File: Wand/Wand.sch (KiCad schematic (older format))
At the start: 27 parts, among them IC1 ATMEGA328-MMH, J1 ACJS-NH35, P1 ISP, P2 BASE, U1 OPA336U, U2 MPU-6050, Y1 16MHz

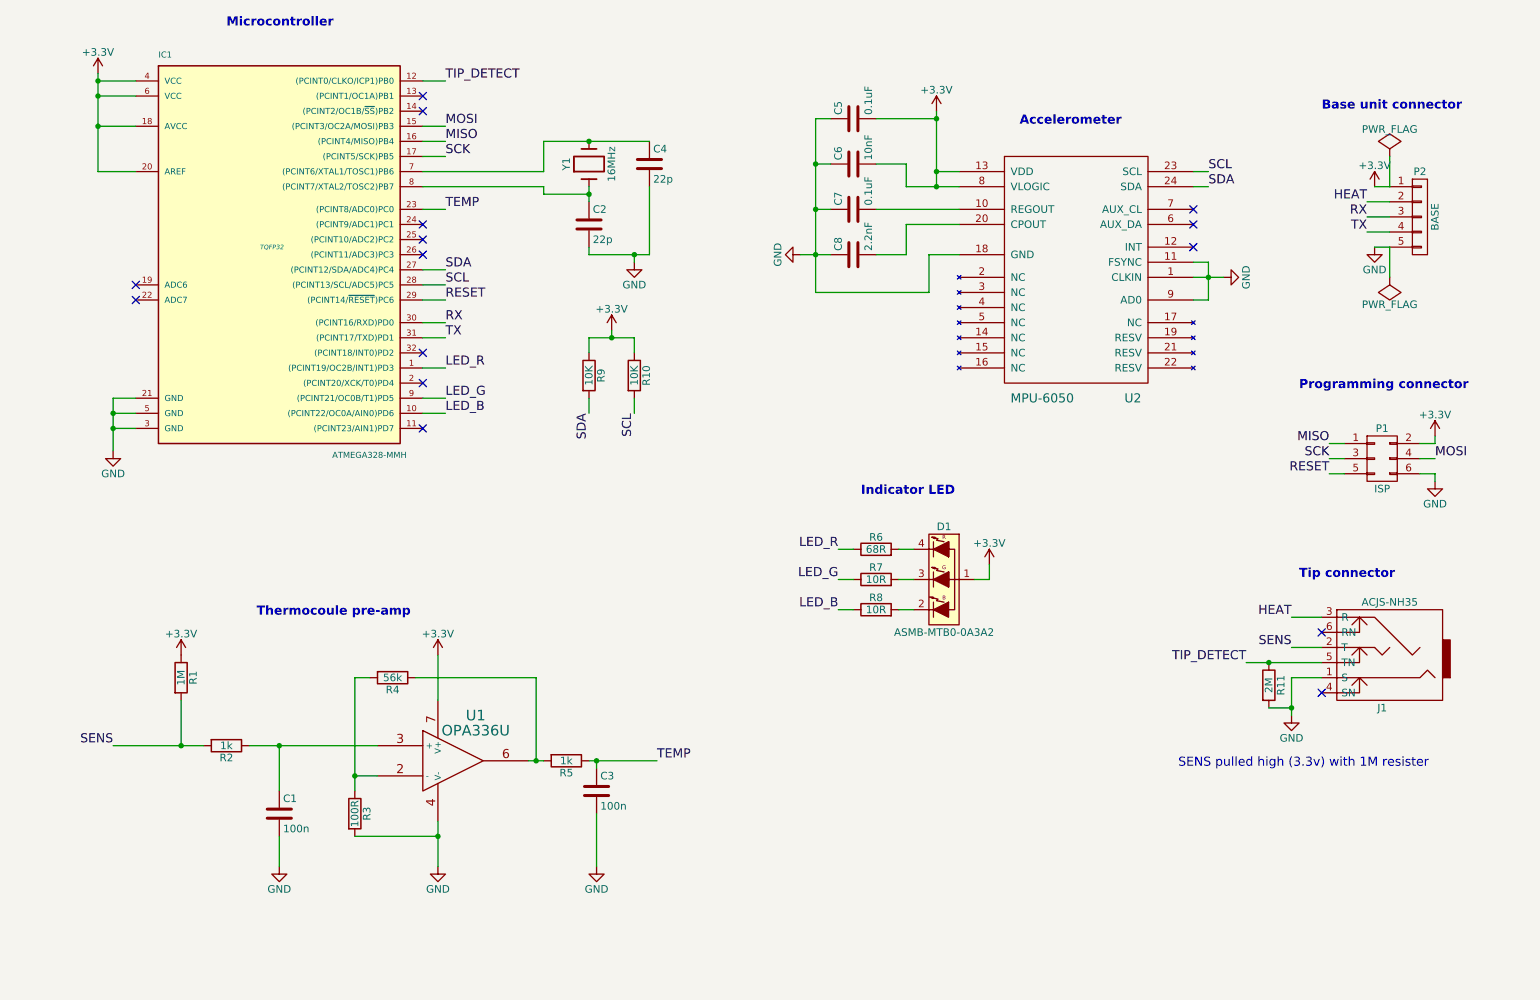
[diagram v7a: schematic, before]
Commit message: Added TMP100 temp sensor to measure the temp at the cold junction.
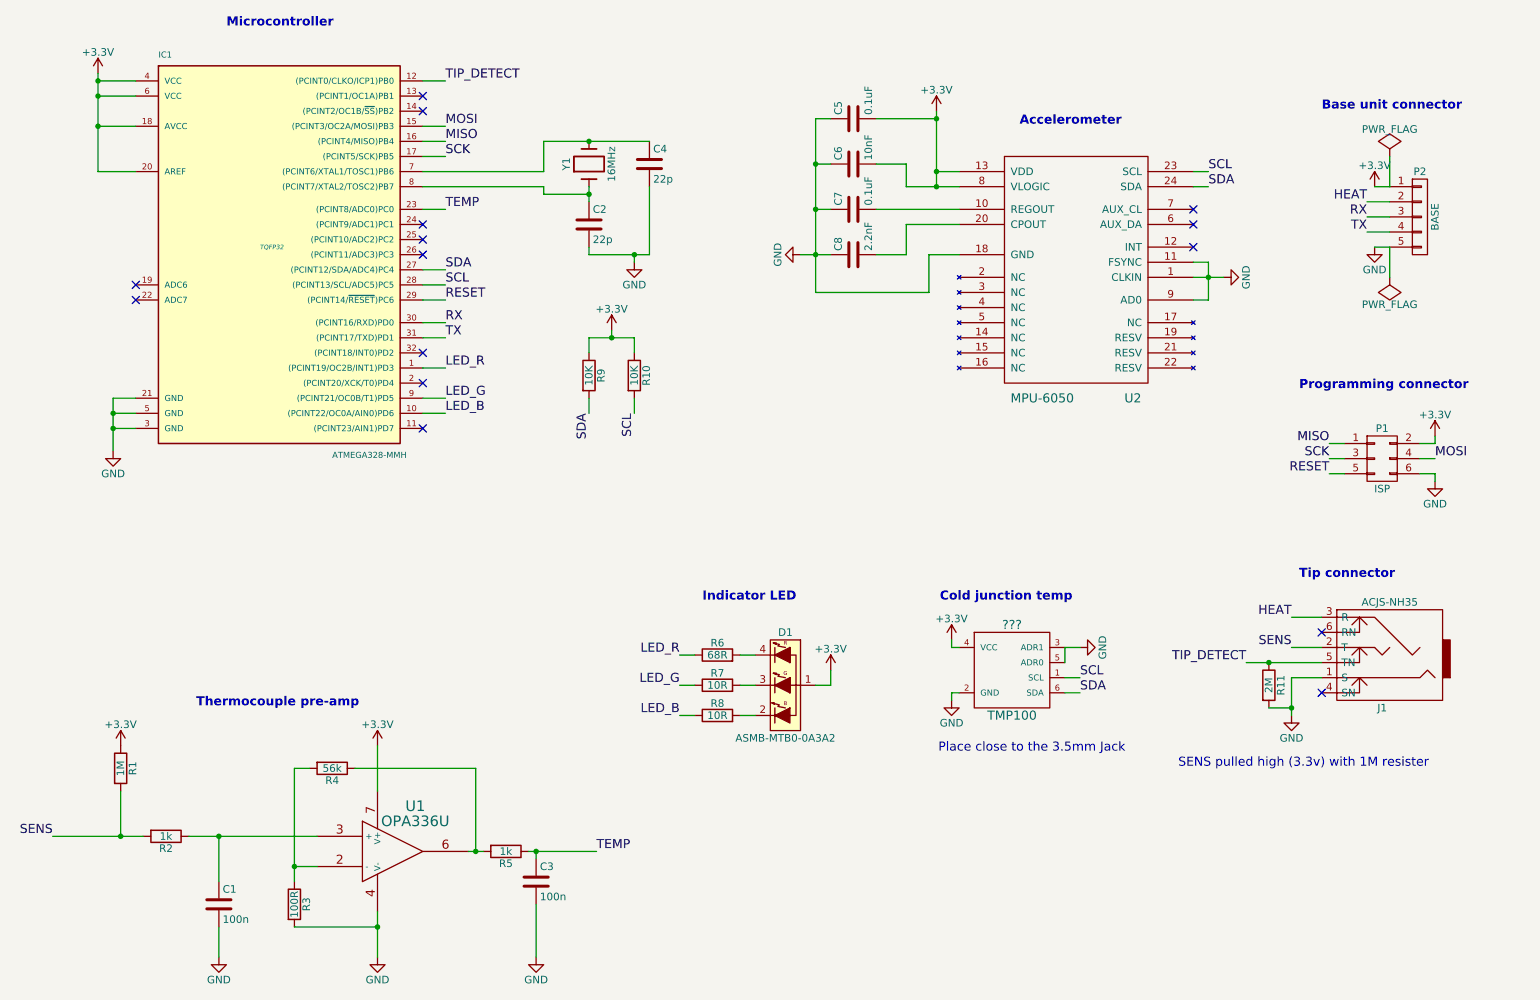
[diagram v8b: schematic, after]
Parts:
- added ???: TMP100, symbol TMP100
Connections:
- net +3V3: now also ???.4 (VCC)
- net GND: now also ???.2 (GND), ???.3 (ADR1), ???.5 (ADR0)
- net SCL: now also ???.1 (SCL)
- net SDA: now also ???.6 (SDA)
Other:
- note added: "Cold junction temp"
- note added: "Place close to the 3.5mm Jack"
- note added: "Thermocouple pre-amp"
- note removed: "Thermocoule pre-amp"
- moved on the sheet: C1, C3, D1, R1, R2, R3, R4, R5, R6, R7, R8, U1
